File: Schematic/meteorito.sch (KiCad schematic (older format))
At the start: 10 parts, among them P1 DH22, P2 GY-ML8511, P3 BMP180

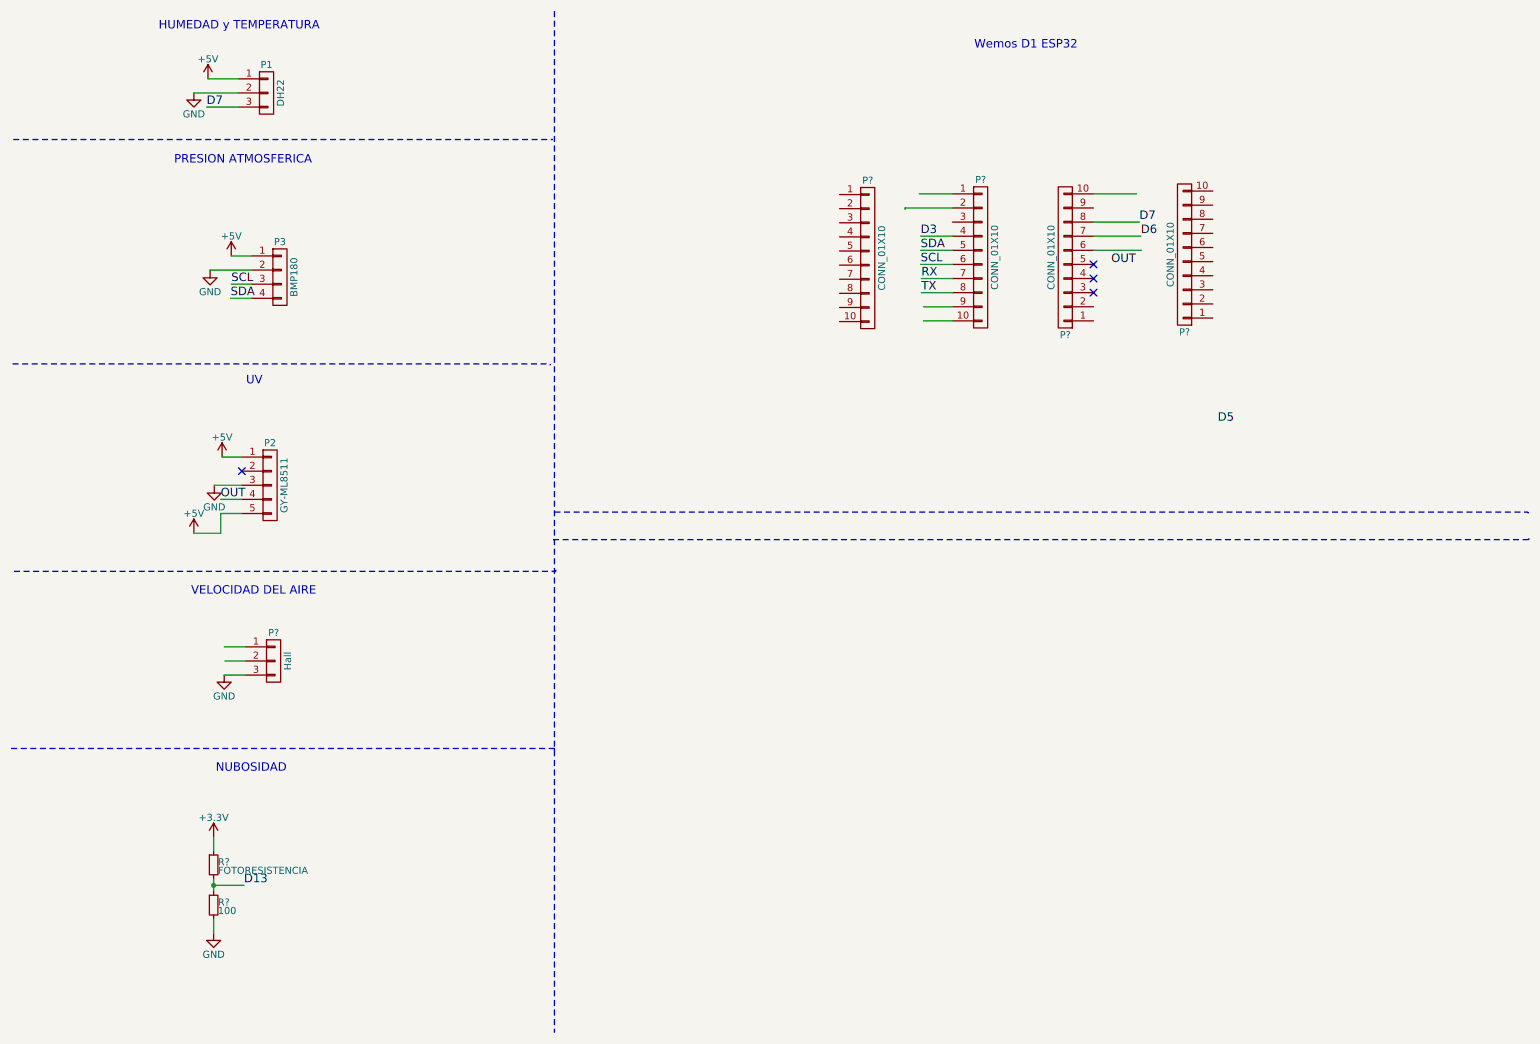
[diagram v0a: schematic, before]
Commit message: Actualización de pines
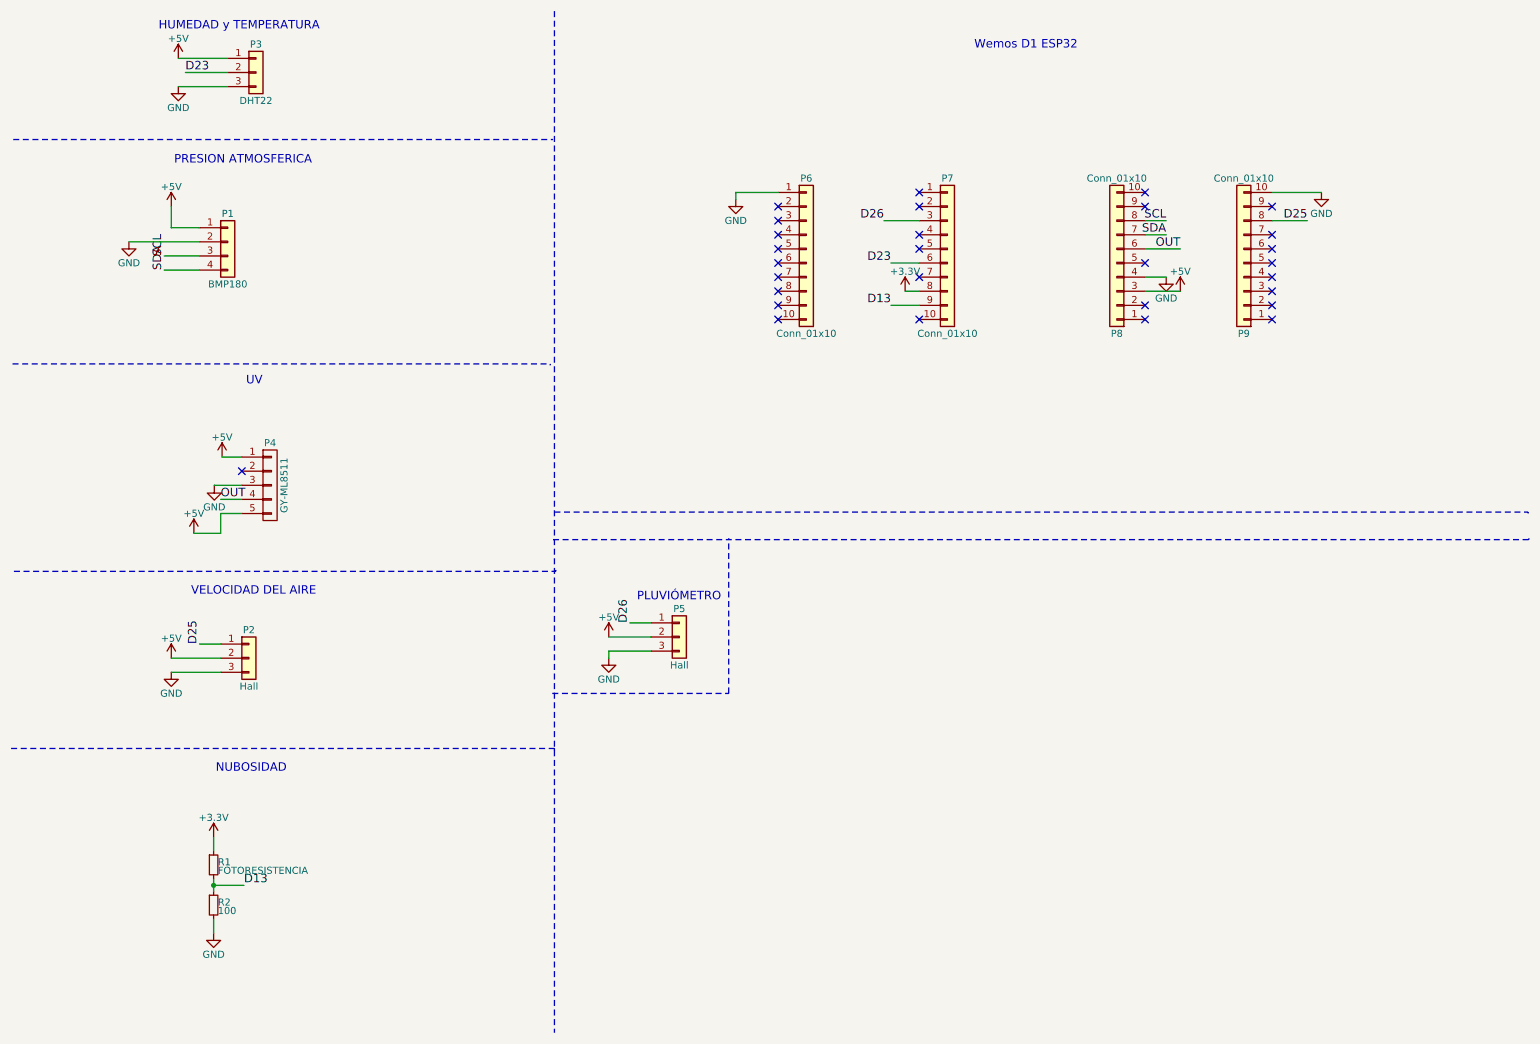
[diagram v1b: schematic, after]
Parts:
- removed P1: DH22, Pin_Headers:Pin_Header_Straight_1x03_Pitch2.54mm, symbol CONN_01X03
- removed P3: BMP180, Pin_Headers:Pin_Header_Straight_1x04_Pitch2.54mm, symbol CONN_01X04
- removed P?: Hall, symbol CONN_01X03
- removed P? (x4): CONN_01X10, symbol CONN_01X10
- added P1: BMP180, symbol Conn_01x04
- added P2, P5: Hall, symbol Conn_01x03
- added P3: DHT22, symbol Conn_01x03
- added P6, P7, P8, P9: Conn_01x10, symbol Conn_01x10
- gave numbers to parts that had none: 2
- renumbered P2 to P4
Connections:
- net labels added: D23, D25, D26
- net labels removed: D3, D5, D6, D7, RX, TX
- wire segments 36 -> 39
- no-connect marks 4 -> 29
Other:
- note added: "PLUVIÓMETRO\n"
